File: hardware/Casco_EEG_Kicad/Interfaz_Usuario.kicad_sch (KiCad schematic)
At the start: 5 parts, among them SW5 SW_Push, SW6 SW_Nidec_CAS-120A1

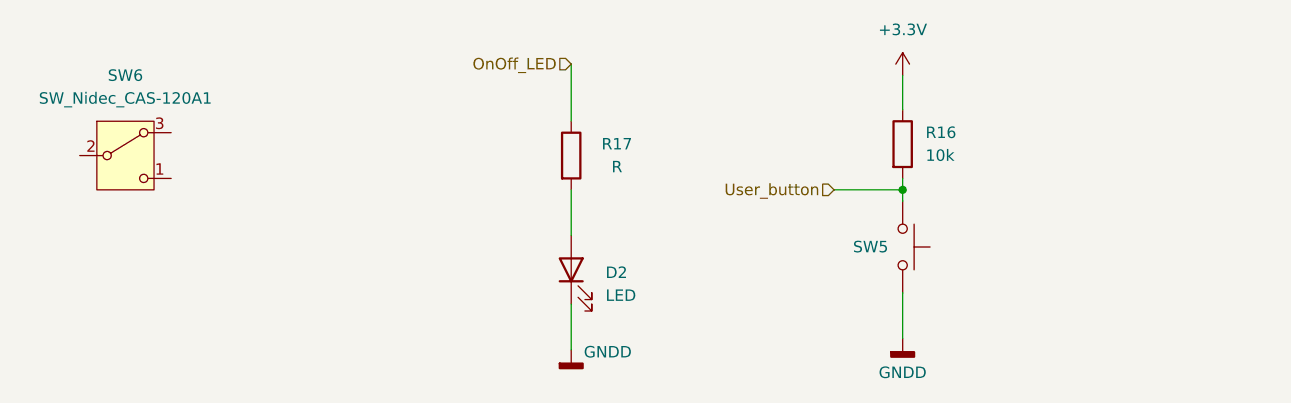
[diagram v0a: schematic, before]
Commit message: Primera implementacion de PCB, cambios varios
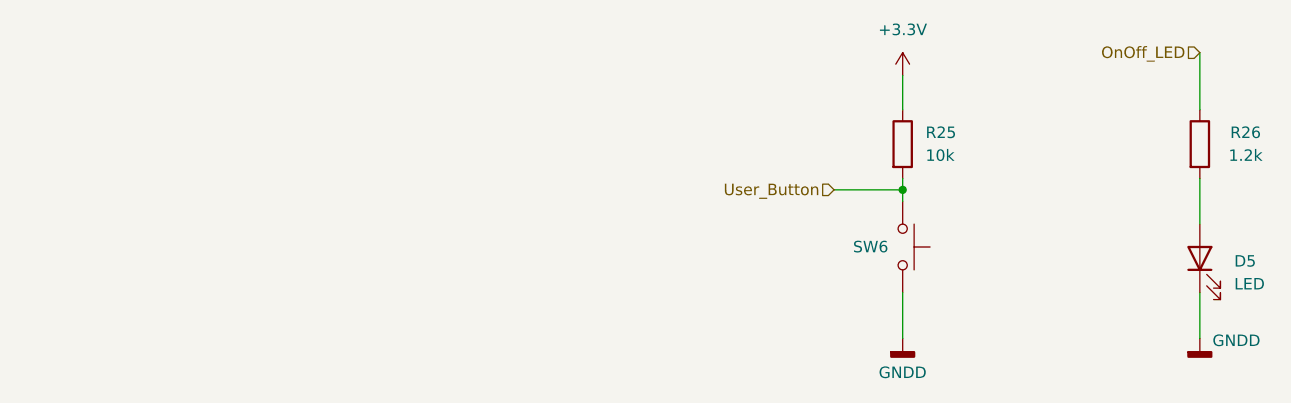
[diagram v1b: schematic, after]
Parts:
- removed SW6: SW_Nidec_CAS-120A1, Button_Switch_SMD:Nidec_Copal_CAS-120A, symbol Switch:SW_Nidec_CAS-120A1
- D5: renamed from D2; footprint (none) -> LED_SMD:LED_0603_1608Metric
- R25: renamed from R16; footprint (none) -> Resistor_SMD:R_0603_1608Metric
- R26: renamed from R17; value R -> 1.2k; footprint (none) -> Resistor_SMD:R_0603_1608Metric
- SW6: renamed from SW5; footprint (none) -> Button_Switch_SMD:SW_SPST_TL3305A
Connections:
- net User_button renamed User_Button
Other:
- moved on the sheet: D5, R26
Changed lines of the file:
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@@
 	(wire
 		(pts
-			(xy 111.76 95.25) (xy 111.76 100.33)
+			(xy 181.61 93.98) (xy 181.61 99.06)
 		)
 		(stroke
@@
 	(wire
 		(pts
-			(xy 111.76 81.28) (xy 111.76 87.63)
+			(xy 181.61 80.01) (xy 181.61 86.36)
 		)
 		(stroke
@@
 	(wire
 		(pts
-			(xy 111.76 113.03) (xy 111.76 107.95)
+			(xy 181.61 111.76) (xy 181.61 106.68)
 		)
 		(stroke
@@
 	(hierarchical_label "OnOff_LED"
 		(shape input)
-		(at 111.76 81.28 180)
+		(at 181.61 80.01 180)
 		(effects
 			(font
@@
 		)
 	)
-	(hierarchical_label "User_button"
+	(hierarchical_label "User_Button"
 		(shape input)
 		(at 140.97 95.25 180)
@@
 	)
 	(symbol
-		(lib_id "Switch:SW_Nidec_CAS-120A1")
-		(at 62.23 91.44 0)
-		(unit 1)
-		(exclude_from_sim no)
-		(in_bom yes)
-		(on_board yes)
-		(dnp no)
-		(fields_autoplaced yes)
-		(property "Reference" "SW6"
-			(at 62.23 82.55 0)
-			(effects
-				(font
-					(size 1.27 1.27)
-				)
-			)
-		)
-		(property "Value" "SW_Nidec_CAS-120A1"
-			(at 62.23 85.09 0)
-			(effects
-				(font
-					(size 1.27 1.27)
-				)
-			)
-		)
-		(property "Footprint" "Button_Switch_SMD:Nidec_Copal_CAS-120A"
-			(at 62.23 101.6 0)
-			(effects
-				(font
-					(size 1.27 1.27)
-				)
-				(hide yes)
-			)
-		)
-		(property "Datasheet" "https://www.nidec-components.com/e/catalog/switch/cas.pdf"
-			(at 62.23 99.06 0)
-			(effects
-				(font
-					(size 1.27 1.27)
-				)
-				(hide yes)
-			)
-		)
-		(property "Description" "Switch, single pole double throw"
-			(at 62.23 91.44 0)
-			(effects
-				(font
-					(size 1.27 1.27)
-				)
-				(hide yes)
-			)
-		)
-		(pin "3"
-		)
-		(pin "2"
-		)
-		(pin "1"
-		)
-		(instances
-			(project ""
-				(path "/3414db36-80da-469c-8b48-81d6bd2f8966/9b4f0b8a-fe97-4a35-b42d-1b02d9df194c"
-					(reference "SW6")
-					(unit 1)
-				)
-			)
-		)
-	)
-	(symbol
 		(lib_id "power:GNDD")
 		(at 148.59 111.76 0)
@@
 		(dnp no)
 		(fields_autoplaced yes)
-		(property "Reference" "#PWR029"
+		(property "Reference" "#PWR044"
 			(at 148.59 118.11 0)
 			(effects
@@
 			(project "Casco_EEG_Kicad"
 				(path "/3414db36-80da-469c-8b48-81d6bd2f8966/9b4f0b8a-fe97-4a35-b42d-1b02d9df194c"
-					(reference "#PWR029")
+					(reference "#PWR044")
 					(unit 1)
 				)
@@
 	(symbol
 		(lib_id "Device:R")
-		(at 111.76 91.44 0)
-		(unit 1)
-		(exclude_from_sim no)
-		(in_bom yes)
-		(on_board yes)
-		(dnp no)
-		(property "Reference" "R17"
-			(at 116.84 90.17 0)
-			(effects
-				(font
-					(size 1.27 1.27)
-				)
-			)
-		)
-		(property "Value" "R"
-			(at 116.84 92.71 0)
+		(at 181.61 90.17 0)
+		(unit 1)
+		(exclude_from_sim no)
+		(in_bom yes)
+		(on_board yes)
+		(dnp no)
+		(property "Reference" "R26"
+			(at 186.69 88.9 0)
+			(effects
+				(font
+					(size 1.27 1.27)
+				)
+			)
+		)
+		(property "Value" "1.2k"
+			(at 186.69 91.44 0)
+			(effects
+				(font
+					(size 1.27 1.27)
+				)
+			)
+		)
+		(property "Footprint" "Resistor_SMD:R_0603_1608Metric"
+			(at 179.832 90.17 90)
+			(effects
+				(font
+					(size 1.27 1.27)
+				)
+				(hide yes)
+			)
+		)
+		(property "Datasheet" "~"
+			(at 181.61 90.17 0)
+			(effects
+				(font
+					(size 1.27 1.27)
+				)
+				(hide yes)
+			)
+		)
+		(property "Description" "Resistor"
+			(at 181.61 90.17 0)
+			(effects
+				(font
+					(size 1.27 1.27)
+				)
+				(hide yes)
+			)
+		)
+		(pin "2"
+		)
+		(pin "1"
+		)
+		(instances
+			(project "Casco_EEG_Kicad"
+				(path "/3414db36-80da-469c-8b48-81d6bd2f8966/9b4f0b8a-fe97-4a35-b42d-1b02d9df194c"
+					(reference "R26")
+					(unit 1)
+				)
+			)
+		)
+	)
+	(symbol
+		(lib_id "power:GNDD")
+		(at 181.61 111.76 0)
+		(unit 1)
+		(exclude_from_sim no)
+		(in_bom yes)
+		(on_board yes)
+		(dnp no)
+		(property "Reference" "#PWR045"
+			(at 181.61 118.11 0)
+			(effects
+				(font
+					(size 1.27 1.27)
+				)
+				(hide yes)
+			)
+		)
+		(property "Value" "GNDD"
+			(at 185.674 112.014 0)
 			(effects
 				(font
@@
 		)
 		(property "Footprint" ""
-			(at 109.982 91.44 90)
-			(effects
-				(font
-					(size 1.27 1.27)
-				)
-				(hide yes)
-			)
-		)
-		(property "Datasheet" "~"
-			(at 111.76 91.44 0)
-			(effects
-				(font
-					(size 1.27 1.27)
-				)
-				(hide yes)
-			)
-		)
-		(property "Description" "Resistor"
-			(at 111.76 91.44 0)
-			(effects
-				(font
-					(size 1.27 1.27)
-				)
-				(hide yes)
-			)
-		)
-		(pin "2"
-		)
-		(pin "1"
-		)
-		(instances
-			(project "Casco_EEG_Kicad"
-				(path "/3414db36-80da-469c-8b48-81d6bd2f8966/9b4f0b8a-fe97-4a35-b42d-1b02d9df194c"
-					(reference "R17")
-					(unit 1)
-				)
-			)
-		)
-	)
-	(symbol
-		(lib_id "power:GNDD")
-		(at 111.76 113.03 0)
-		(unit 1)
-		(exclude_from_sim no)
-		(in_bom yes)
-		(on_board yes)
-		(dnp no)
-		(property "Reference" "#PWR030"
-			(at 111.76 119.38 0)
-			(effects
-				(font
-					(size 1.27 1.27)
-				)
-				(hide yes)
-			)
-		)
-		(property "Value" "GNDD"
-			(at 115.824 113.284 0)
-			(effects
-				(font
-					(size 1.27 1.27)
-				)
-			)
-		)
-		(property "Footprint" ""
-			(at 111.76 113.03 0)
+			(at 181.61 111.76 0)
 			(effects
 				(font
@@
 		)
 		(property "Datasheet" ""
-			(at 111.76 113.03 0)
+			(at 181.61 111.76 0)
 			(effects
 				(font
@@
 		)
 		(property "Description" "Power symbol creates a global label with name \"GNDD\" , digital ground"
-			(at 111.76 113.03 0)
-			(effects
-				(font
-					(size 1.27 1.27)
-				)
-				(hide yes)
-			)
-		)
-		(pin "1"
-		)
-		(instances
-			(project "Casco_EEG_Kicad"
-				(path "/3414db36-80da-469c-8b48-81d6bd2f8966/9b4f0b8a-fe97-4a35-b42d-1b02d9df194c"
-					(reference "#PWR030")
+			(at 181.61 111.76 0)
+			(effects
+				(font
+					(size 1.27 1.27)
+				)
+				(hide yes)
+			)
+		)
+		(pin "1"
+		)
+		(instances
+			(project "Casco_EEG_Kicad"
+				(path "/3414db36-80da-469c-8b48-81d6bd2f8966/9b4f0b8a-fe97-4a35-b42d-1b02d9df194c"
+					(reference "#PWR045")
 					(unit 1)
 				)
@@
 		(dnp no)
 		(fields_autoplaced yes)
-		(property "Reference" "#PWR028"
+		(property "Reference" "#PWR043"
 			(at 148.59 86.36 0)
 			(effects
@@
 			(project "Casco_EEG_Kicad"
 				(path "/3414db36-80da-469c-8b48-81d6bd2f8966/9b4f0b8a-fe97-4a35-b42d-1b02d9df194c"
-					(reference "#PWR028")
+					(reference "#PWR043")
 					(unit 1)
 				)
@@
 		(dnp no)
 		(fields_autoplaced yes)
-		(property "Reference" "R16"
+		(property "Reference" "R25"
 			(at 151.13 88.8999 0)
 			(effects
@@
 			)
 		)
-		(property "Footprint" ""
+		(property "Footprint" "Resistor_SMD:R_0603_1608Metric"
 			(at 146.812 90.17 90)
 			(effects
@@
 			(project "Casco_EEG_Kicad"
 				(path "/3414db36-80da-469c-8b48-81d6bd2f8966/9b4f0b8a-fe97-4a35-b42d-1b02d9df194c"
-					(reference "R16")
+					(reference "R25")
 					(unit 1)
 				)
@@
 	(symbol
 		(lib_id "Device:LED")
-		(at 111.76 104.14 90)
-		(unit 1)
-		(exclude_from_sim no)
-		(in_bom yes)
-		(on_board yes)
-		(dnp no)
-		(property "Reference" "D2"
-			(at 115.57 104.4574 90)
+		(at 181.61 102.87 90)
+		(unit 1)
+		(exclude_from_sim no)
+		(in_bom yes)
+		(on_board yes)
+		(dnp no)
+		(property "Reference" "D5"
+			(at 185.42 103.1874 90)
 			(effects
 				(font
@@
 		)
 		(property "Value" "LED"
-			(at 115.57 106.9974 90)
+			(at 185.42 105.7274 90)
 			(effects
 				(font
@@
 			)
 		)
-		(property "Footprint" ""
-			(at 111.76 104.14 0)
+		(property "Footprint" "LED_SMD:LED_0603_1608Metric"
+			(at 181.61 102.87 0)
 			(effects
 				(font
@@
 		)
 		(property "Datasheet" "~"
-			(at 111.76 104.14 0)
+			(at 181.61 102.87 0)
 			(effects
 				(font
@@
 		)
 		(property "Description" "Light emitting diode"
-			(at 111.76 104.14 0)
+			(at 181.61 102.87 0)
 			(effects
 				(font
@@
 		)
 		(property "Sim.Pins" "1=K 2=A"
-			(at 111.76 104.14 0)
+			(at 181.61 102.87 0)
 			(effects
 				(font
@@
 			(project "Casco_EEG_Kicad"
 				(path "/3414db36-80da-469c-8b48-81d6bd2f8966/9b4f0b8a-fe97-4a35-b42d-1b02d9df194c"
-					(reference "D2")
+					(reference "D5")
 					(unit 1)
 				)
@@
 		(on_board yes)
 		(dnp no)
-		(property "Reference" "SW5"
+		(property "Reference" "SW6"
 			(at 145.034 101.6 90)
 			(effects
@@
 			)
 		)
-		(property "Footprint" ""
+		(property "Footprint" "Button_Switch_SMD:SW_SPST_TL3305A"
 			(at 153.67 101.6 0)
 			(effects
@@
 			(project "Casco_EEG_Kicad"
 				(path "/3414db36-80da-469c-8b48-81d6bd2f8966/9b4f0b8a-fe97-4a35-b42d-1b02d9df194c"
-					(reference "SW5")
-					(unit 1)
-				)
+					(reference "SW6")
+					(unit 1)
+				)

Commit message: Nuevos cambios al PCB, mejoro planos, regulo 3,3V desde 5V, etc
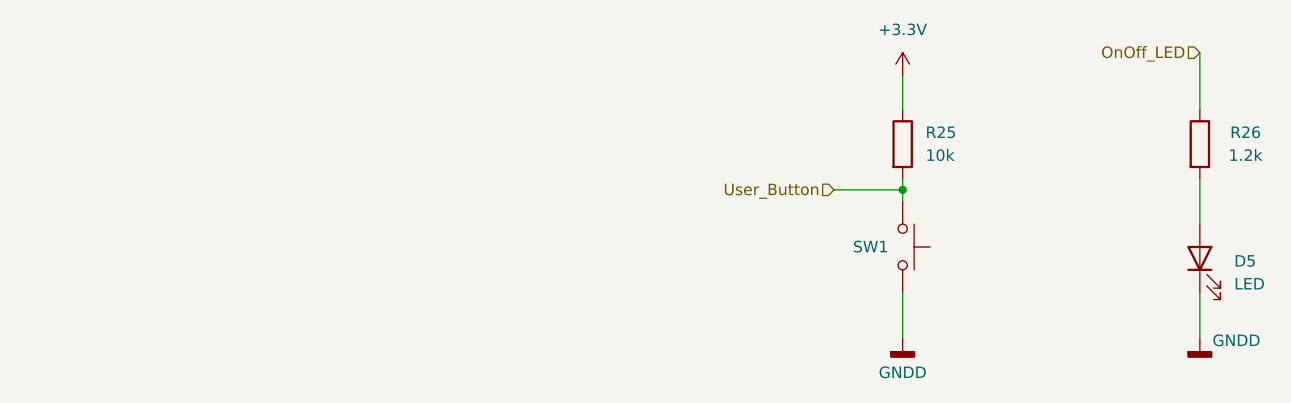
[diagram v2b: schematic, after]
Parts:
- R25: LCSC PN (none) -> C25804
- R26: LCSC PN (none) -> C22765
- renumbered SW6 to SW1
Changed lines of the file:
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@@
+			)
+		)
+		(property "LCSC PN" "C22765"
+			(at 181.61 90.17 0)
+			(effects
+				(font
+					(size 1.27 1.27)
+				)
+				(hide yes)
 			)
 		)
@@
 			)
 		)
+		(property "LCSC PN" "C25804"
+			(at 148.59 90.17 0)
+			(effects
+				(font
+					(size 1.27 1.27)
+				)
+				(hide yes)
+			)
+		)
 		(pin "1"
 		)
@@
 		(on_board yes)
 		(dnp no)
-		(property "Reference" "SW6"
+		(property "Reference" "SW1"
 			(at 145.034 101.6 90)
 			(effects
@@
 			(project "Casco_EEG_Kicad"
 				(path "/3414db36-80da-469c-8b48-81d6bd2f8966/9b4f0b8a-fe97-4a35-b42d-1b02d9df194c"
-					(reference "SW6")
-					(unit 1)
-				)
+					(reference "SW1")
+					(unit 1)
+				)
